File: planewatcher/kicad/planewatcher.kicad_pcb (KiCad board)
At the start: 4 copper layers, 86.1 x 54 mm, 156 parts, among them J1 1PPS_OUT, J2 RF_IN, J3 BMI-S-209-F + C, J4 FPGA BANK 33, J5 FPGA BANK 35 V1.2/V1.3, J6 GPS _IN, U1 LEA-M8T, U10 AD8138, U11 AD9203, U2 AP22653AW6-7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

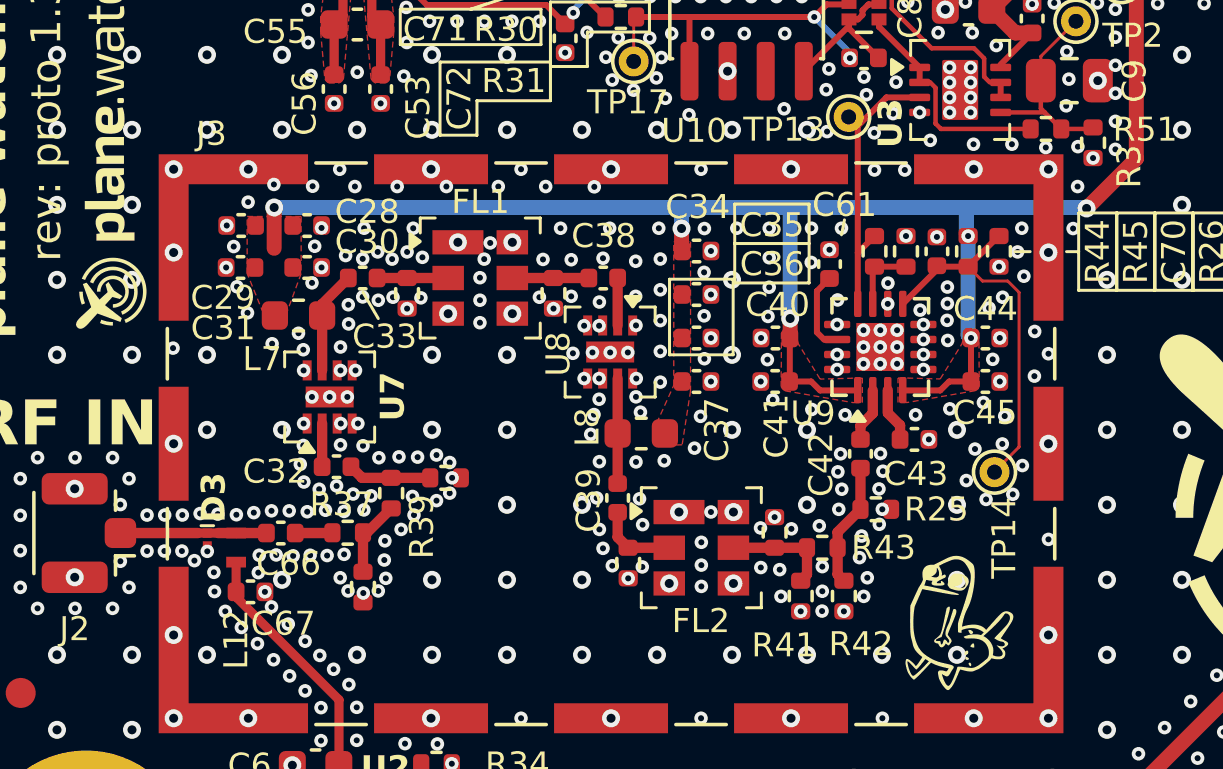
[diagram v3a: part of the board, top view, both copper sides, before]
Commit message: Tighten up RF section layout
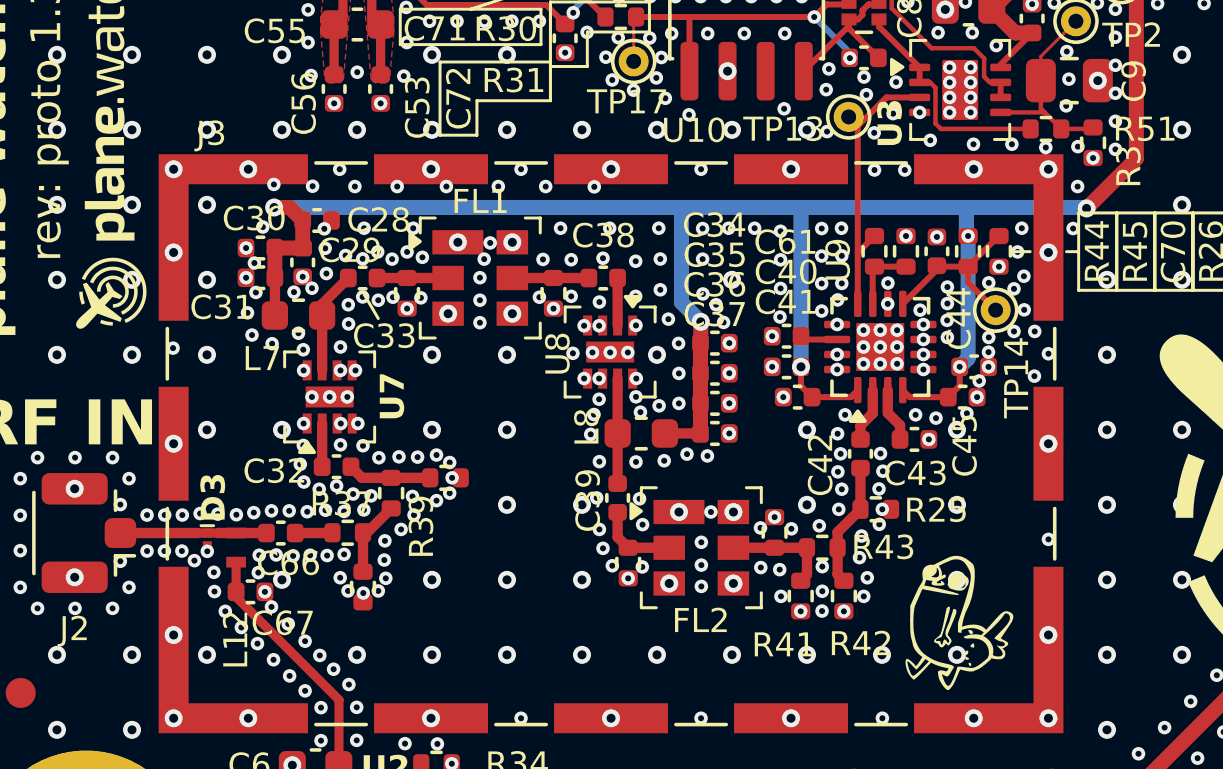
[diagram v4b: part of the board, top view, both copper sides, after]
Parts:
- moved TP14 5.40 mm to (141.3, 96.0)
- moved C34 3.13 mm to (131.9, 97.1)
- moved C61 2.80 mm to (134.3, 96.9), turned to 0 degrees
- moved C35 2.70 mm to (131.9, 98.1)
- moved C29 2.39 mm to (118.2, 94.4), turned to -90 degrees
- moved C36 2.26 mm to (131.9, 99.1)
- moved C37 1.84 mm to (131.9, 100.1)
- moved C30 1.68 mm to (116.8, 93.9), turned to 180 degrees
- moved C44 1.03 mm to (140.6, 97.9)
- moved C40 1.03 mm to (134.3, 97.9)
- moved C45 0.92 mm to (140.2, 98.9)
- moved C41 0.91 mm to (134.7, 98.9)
- moved C31 0.75 mm to (116.8, 94.9)
- moved C28 0.37 mm to (118.7, 93.0)
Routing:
- net 3V3A: track 108.4 -> 119.7 mm
- net Net-(U9-TADJ): track 12.6 -> 6.08 mm
- net Net-(U9-CLPF): track 2.74 -> 1.25 mm
- net GND: vias 1850 -> 1857
